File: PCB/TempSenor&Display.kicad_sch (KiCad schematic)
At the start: 1 part, among them U4 ACDC02-41SGWA-F01

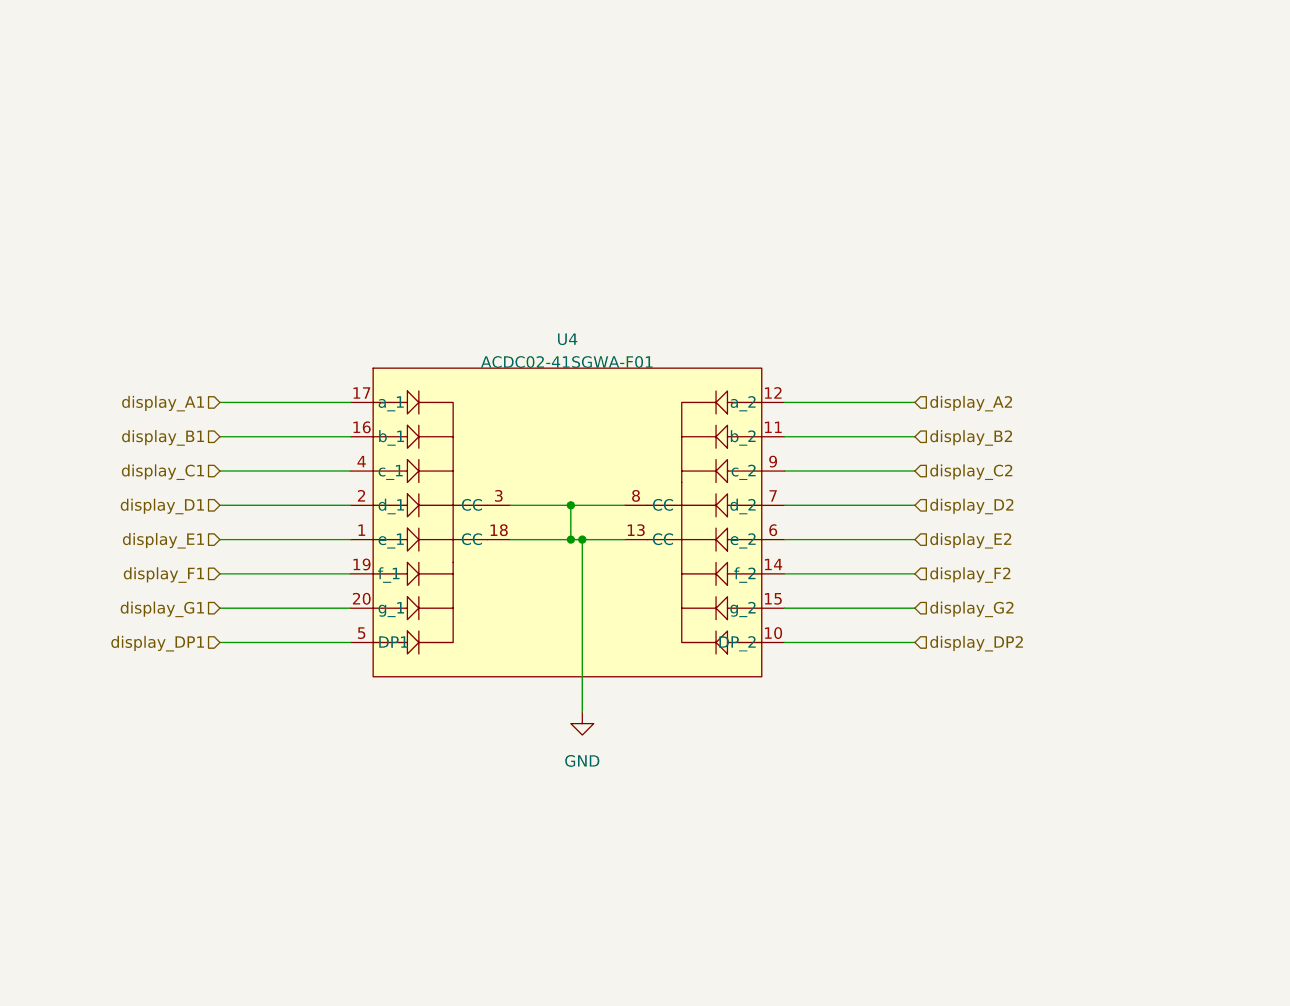
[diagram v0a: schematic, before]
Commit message: Layout complted, gerber files generated
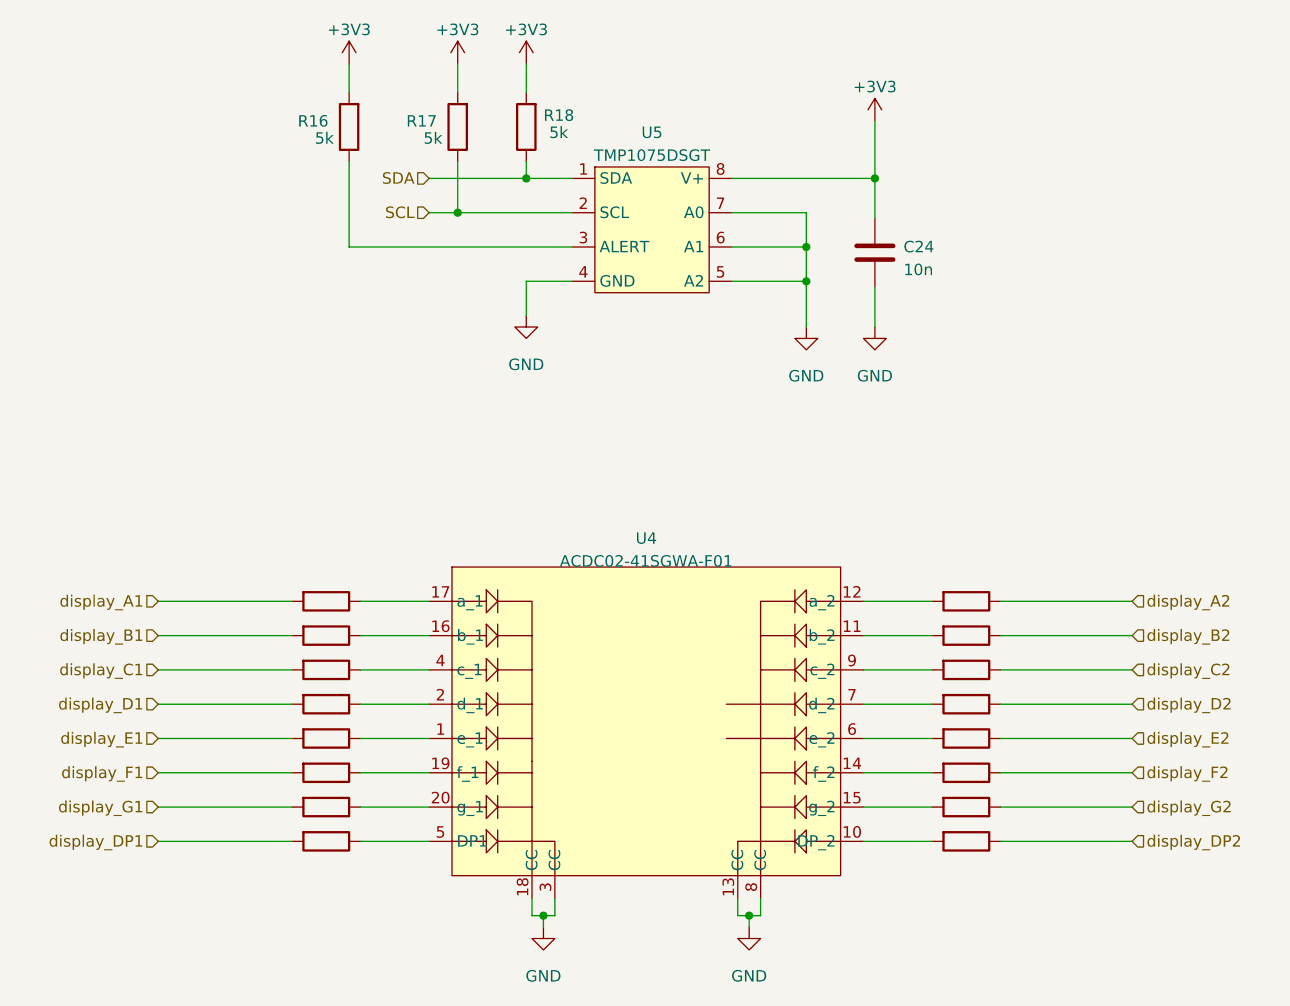
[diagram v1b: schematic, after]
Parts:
- added C24: 10n, Capacitor_SMD:C_0603_1608Metric, symbol Device:C
- added R16, R17, R18, R19, R20, R21, R22, R23, R24, R25, R26, R27, R28, R29, R30, R31, R32, R33, R34: 5k, Resistor_SMD:R_0603_1608Metric, symbol Device:R
- added U5: TMP1075DSGT, Package_SON:WSON-8-1EP_2x2mm_P0.5mm_EP0.9x1.6mm, symbol User_Symbol:TMP1075DSGT
- U4: footprint (none) -> User_Footprint:7DIG_ACDC02-41SGWA-F01
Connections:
- net GND: now also C24.2, U5.4 (GND), U5.5 (A2), U5.6 (A1), U5.7 (A0)
- net display_A1: now also R27.2; no longer U4.17 (a_1)
- net display_A2: now also R19.1; no longer U4.12 (a_2)
- net display_B1: now also R28.2; no longer U4.16 (b_1)
- net display_B2: now also R20.1; no longer U4.11 (b_2)
- net display_C1: now also R29.2; no longer U4.4 (c_1)
- net display_C2: now also R21.1; no longer U4.9 (c_2)
- net display_D1: now also R30.2; no longer U4.2 (d_1)
- net display_D2: now also R22.1; no longer U4.7 (d_2)
- net display_DP1: now also R34.2; no longer U4.5 (DP1)
- net display_DP2: now also R26.1; no longer U4.10 (DP_2)
- net display_E1: now also R31.2; no longer U4.1 (e_1)
- net display_E2: now also R23.1; no longer U4.6 (e_2)
- net display_F1: now also R32.2; no longer U4.19 (f_1)
- net display_F2: now also R24.1; no longer U4.14 (f_2)
- net display_G1: now also R33.2; no longer U4.20 (g_1)
- net display_G2: now also R25.1; no longer U4.15 (g_2)
- new net: R28.1, U4.16 (b_1)
- new net: R16.1, U5.3 (ALERT)
- new net: R29.1, U4.4 (c_1)
- new net: R23.2, U4.6 (e_2)
- new net: R27.1, U4.17 (a_1)
- new net: R32.1, U4.19 (f_1)
- new net: R24.2, U4.14 (f_2)
- new net: R20.2, U4.11 (b_2)
- new net: R33.1, U4.20 (g_1)
- new net: R31.1, U4.1 (e_1)
- new net: R26.2, U4.10 (DP_2)
- new net: R19.2, U4.12 (a_2)
- new net: R25.2, U4.15 (g_2)
- new net: R30.1, U4.2 (d_1)
- new net: R34.1, U4.5 (DP1)
- new net: R22.2, U4.7 (d_2)
- new net: R21.2, U4.9 (c_2)
- new net +3V3: C24.1, R16.2, R17.2, R18.2, U5.8 (V+)
- new net SCL: R17.1, U5.2 (SCL)
- new net SDA: R18.1, U5.1 (SDA)
